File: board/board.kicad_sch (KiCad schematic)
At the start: 0 parts

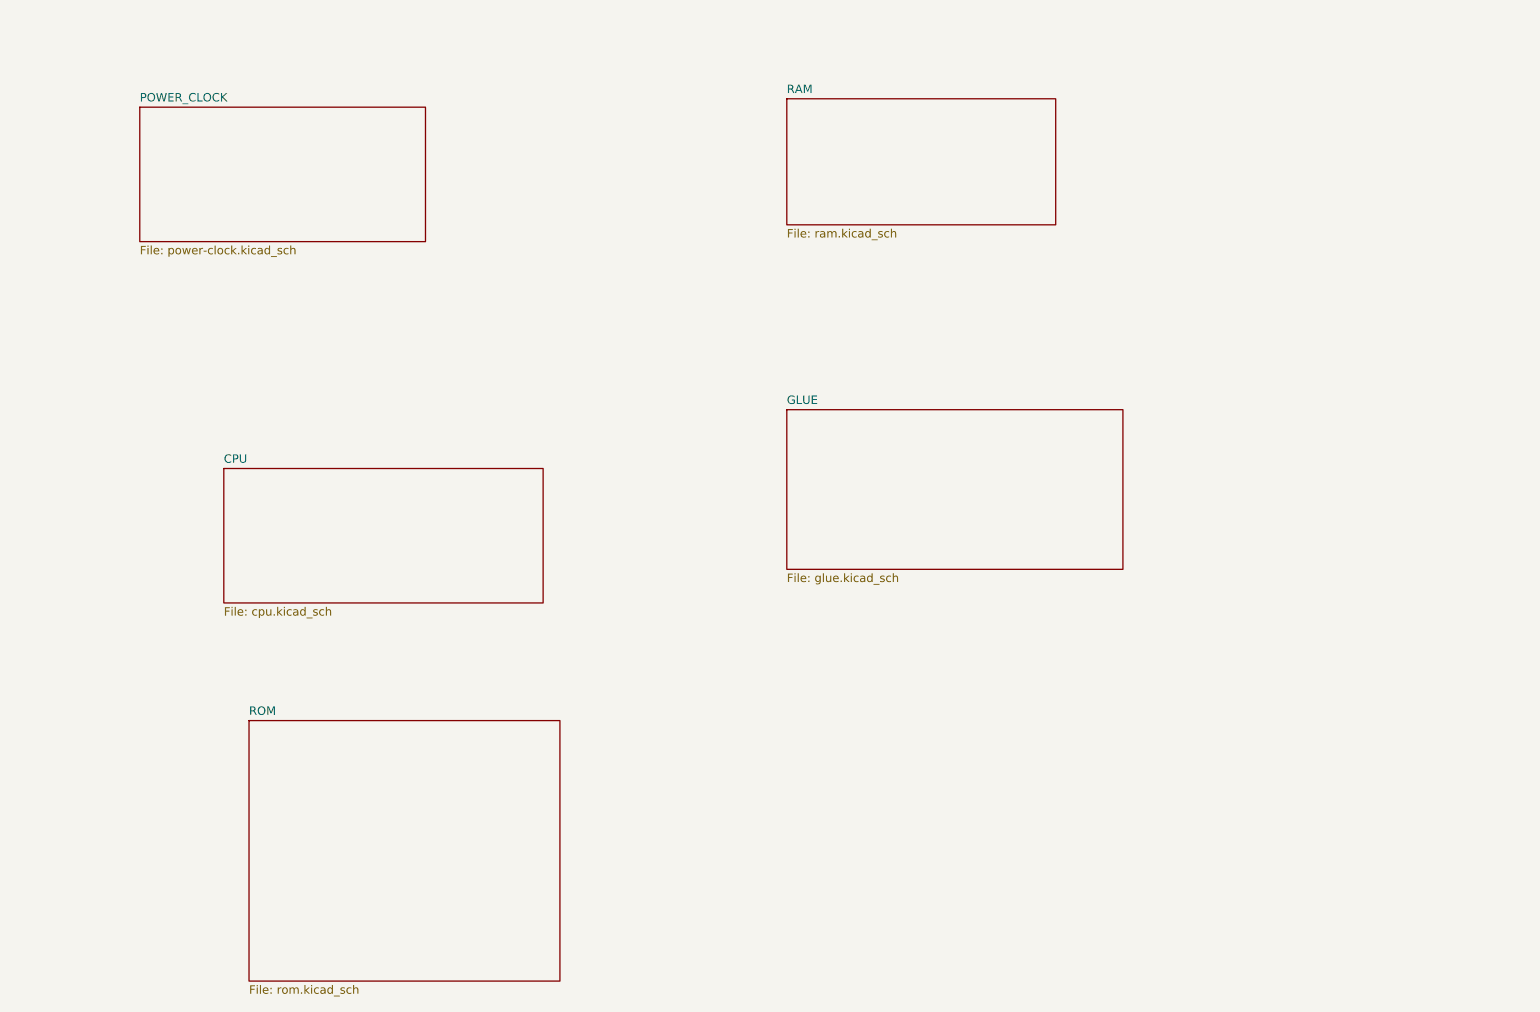
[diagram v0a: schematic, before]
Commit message: fill out most functionality - passes ERC
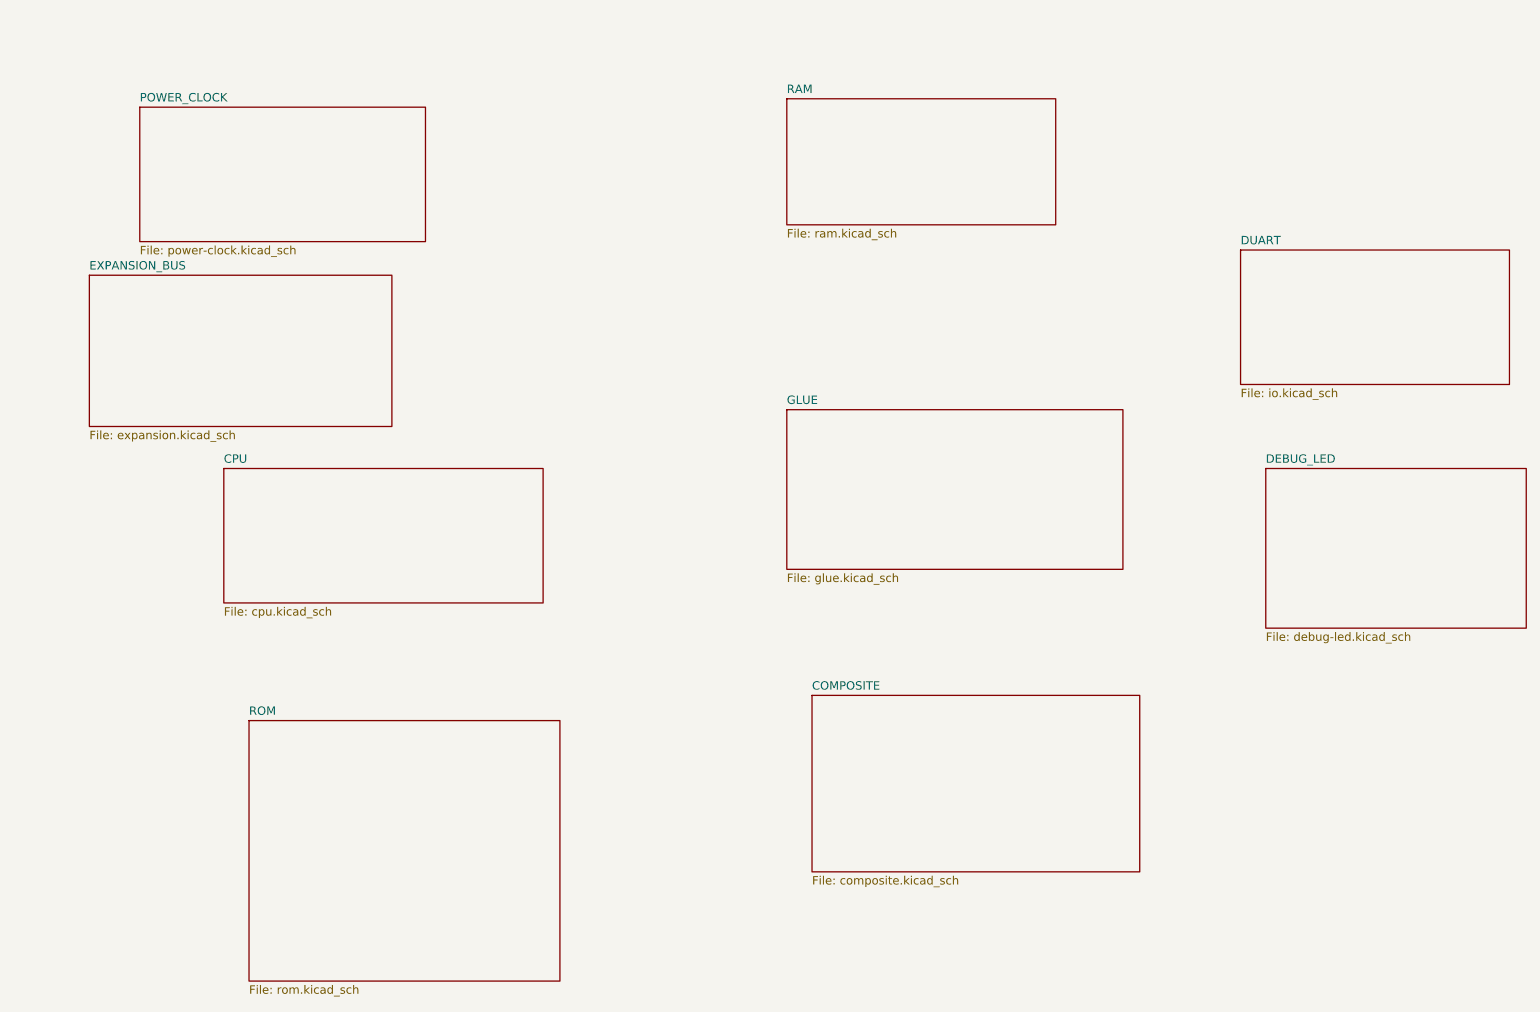
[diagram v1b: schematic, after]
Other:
- added sheet COMPOSITE (composite.kicad_sch)
- added sheet DEBUG_LED (debug-led.kicad_sch)
- added sheet DUART (io.kicad_sch)
- added sheet EXPANSION_BUS (expansion.kicad_sch)
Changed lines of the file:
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@@
+	)
+	(sheet
+		(at 142.24 125.73)
+		(size 49.53 26.67)
+		(exclude_from_sim no)
+		(in_bom yes)
+		(on_board yes)
+		(dnp no)
+		(fields_autoplaced yes)
+		(stroke
+			(width 0.1524)
+			(type solid)
+		)
+		(fill
+			(color 0 0 0 0.0000)
+		)
+		(property "Sheetname" "COMPOSITE"
+			(at 142.24 125.0184 0)
+			(effects
+				(font
+					(size 1.27 1.27)
+				)
+				(justify left bottom)
+			)
+		)
+		(property "Sheetfile" "composite.kicad_sch"
+			(at 142.24 152.9846 0)
+			(effects
+				(font
+					(size 1.27 1.27)
+				)
+				(justify left top)
+			)
+		)
+		(instances
+			(project "board"
+				(path "/afefa398-9f39-4b22-97f8-dae9b102df0d"
+					(page "8")
+				)
+			)
+		)
 	)
 	(sheet
@@
 	)
 	(sheet
+		(at 207.01 58.42)
+		(size 40.64 20.32)
+		(exclude_from_sim no)
+		(in_bom yes)
+		(on_board yes)
+		(dnp no)
+		(fields_autoplaced yes)
+		(stroke
+			(width 0.1524)
+			(type solid)
+		)
+		(fill
+			(color 0 0 0 0.0000)
+		)
+		(property "Sheetname" "DUART"
+			(at 207.01 57.7084 0)
+			(effects
+				(font
+					(size 1.27 1.27)
+				)
+				(justify left bottom)
+			)
+		)
+		(property "Sheetfile" "io.kicad_sch"
+			(at 207.01 79.3246 0)
+			(effects
+				(font
+					(size 1.27 1.27)
+				)
+				(justify left top)
+			)
+		)
+		(instances
+			(project "board"
+				(path "/afefa398-9f39-4b22-97f8-dae9b102df0d"
+					(page "7")
+				)
+			)
+		)
+	)
+	(sheet
+		(at 33.02 62.23)
+		(size 45.72 22.86)
+		(exclude_from_sim no)
+		(in_bom yes)
+		(on_board yes)
+		(dnp no)
+		(fields_autoplaced yes)
+		(stroke
+			(width 0.1524)
+			(type solid)
+		)
+		(fill
+			(color 0 0 0 0.0000)
+		)
+		(property "Sheetname" "EXPANSION_BUS"
+			(at 33.02 61.5184 0)
+			(effects
+				(font
+					(size 1.27 1.27)
+				)
+				(justify left bottom)
+			)
+		)
+		(property "Sheetfile" "expansion.kicad_sch"
+			(at 33.02 85.6746 0)
+			(effects
+				(font
+					(size 1.27 1.27)
+				)
+				(justify left top)
+			)
+		)
+		(instances
+			(project "board"
+				(path "/afefa398-9f39-4b22-97f8-dae9b102df0d"
+					(page "10")
+				)
+			)
+		)
+	)
+	(sheet
 		(at 138.43 35.56)
 		(size 40.64 19.05)
@@
 				)
 			)
+		)
+	)
+	(sheet
+		(at 210.82 91.44)
+		(size 39.37 24.13)
+		(exclude_from_sim no)
+		(in_bom yes)
+		(on_board yes)
+		(dnp no)
+		(fields_autoplaced yes)
+		(stroke
+			(width 0.1524)
+			(type solid)
+		)
+		(fill
+			(color 0 0 0 0.0000)
+		)
+		(property "Sheetname" "DEBUG_LED"
+			(at 210.82 90.7284 0)
+			(effects
+				(font
+					(size 1.27 1.27)
+				)
+				(justify left bottom)
+			)
+		)
+		(property "Sheetfile" "debug-led.kicad_sch"
+			(at 210.82 116.1546 0)
+			(effects
+				(font
+					(size 1.27 1.27)
+				)
+				(justify left top)
+			)
+		)
+		(instances
+			(project "board"
+				(path "/afefa398-9f39-4b22-97f8-dae9b102df0d"
+					(page "9")
+				)
+			)

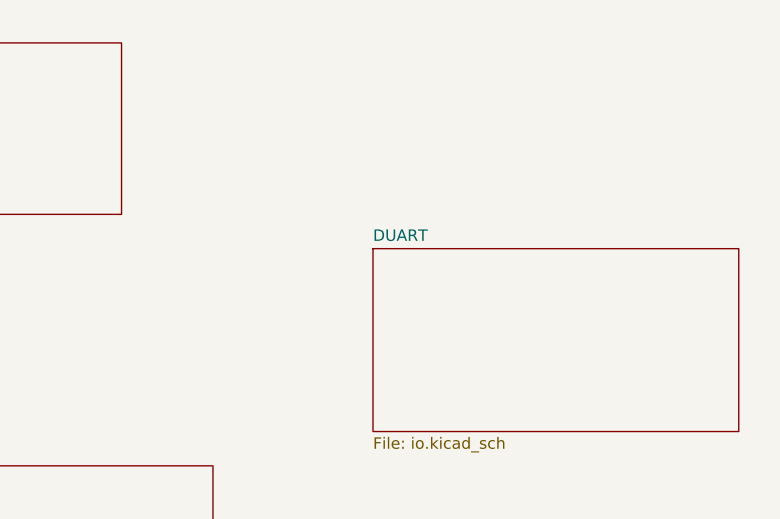
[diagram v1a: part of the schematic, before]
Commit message: change IO to 8051 variant, add audio
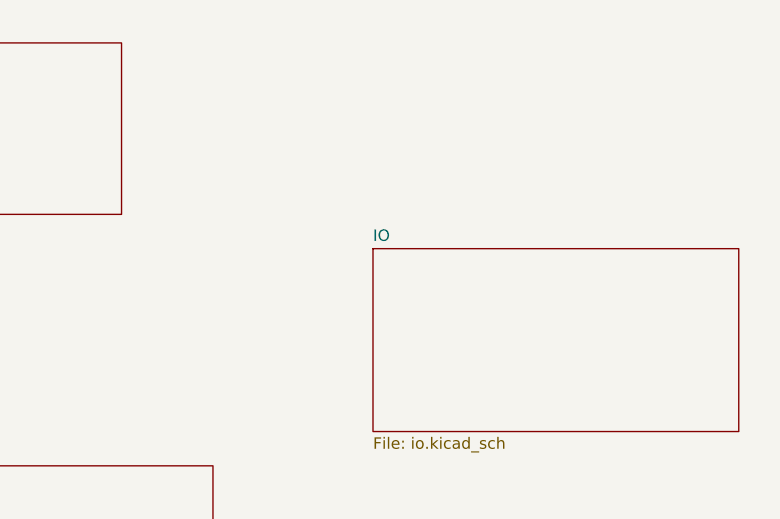
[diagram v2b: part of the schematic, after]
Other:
- sheet DUART renamed IO
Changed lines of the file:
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@@
 			(color 0 0 0 0.0000)
 		)
-		(property "Sheetname" "DUART"
+		(property "Sheetname" "IO"
 			(at 207.01 57.7084 0)
 			(effects

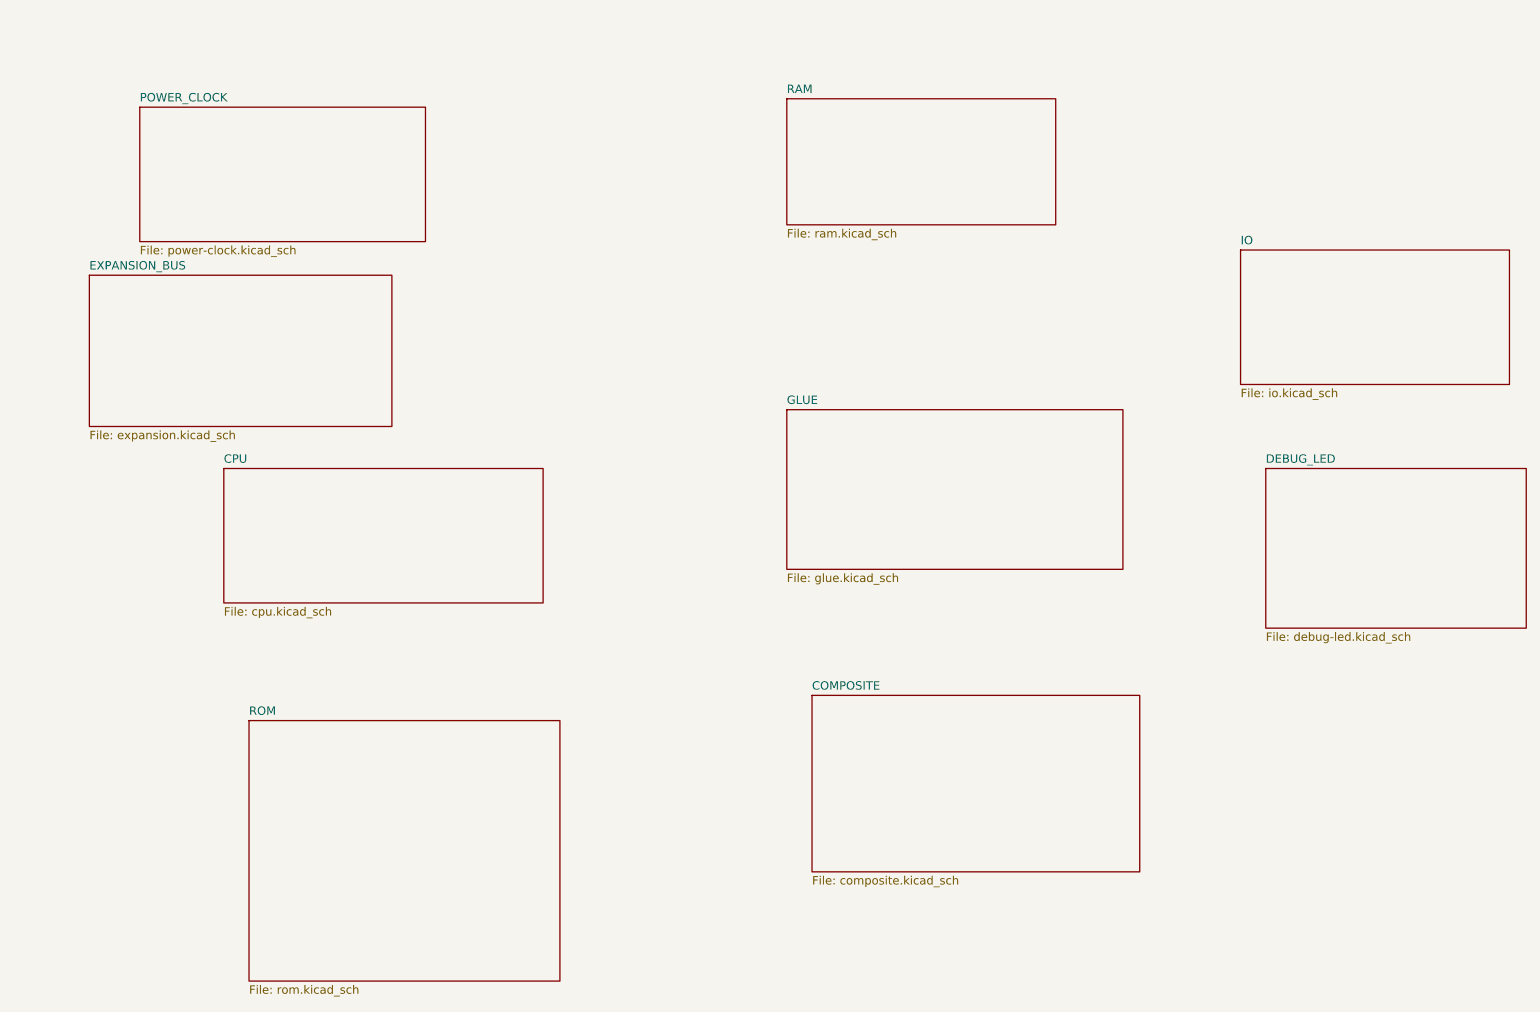
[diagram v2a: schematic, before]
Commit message: start of PCB and MMU
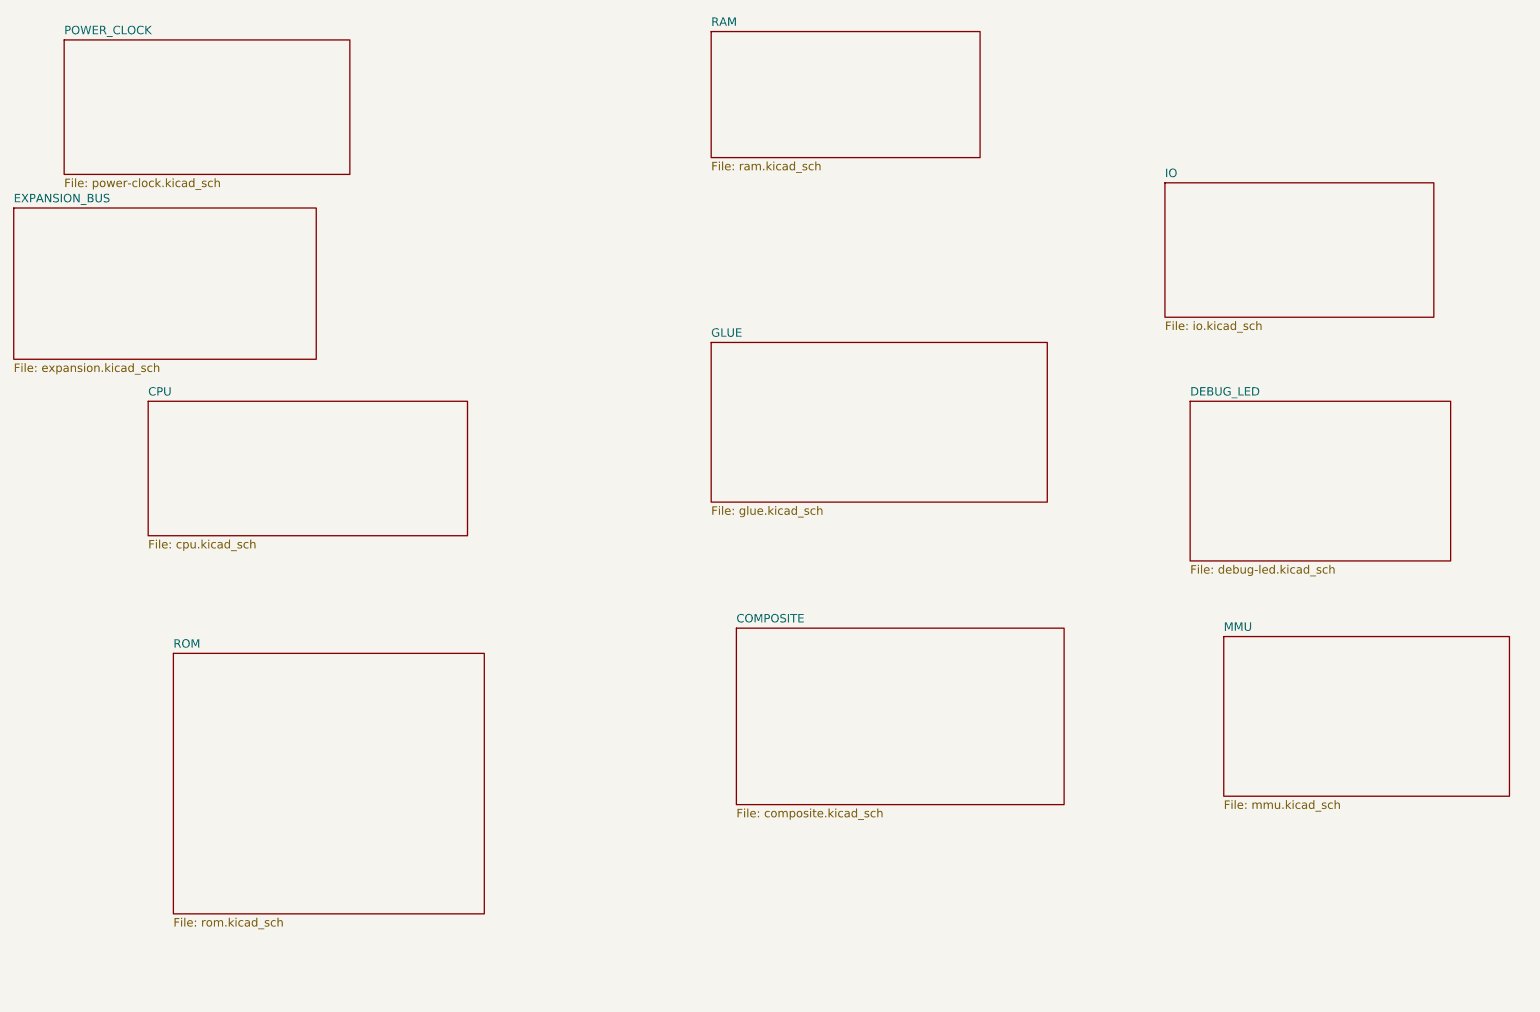
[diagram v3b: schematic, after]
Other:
- added sheet MMU (mmu.kicad_sch)
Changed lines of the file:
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@@
 	(paper "A4")
 	(sheet
-		(at 138.43 82.55)
+		(at 127 72.39)
 		(size 50.8 24.13)
 		(exclude_from_sim no)
@@
 		)
 		(property "Sheetname" "GLUE"
-			(at 138.43 81.8384 0)
+			(at 127 71.6784 0)
 			(effects
 				(font
@@
 		)
 		(property "Sheetfile" "glue.kicad_sch"
-			(at 138.43 107.2646 0)
+			(at 127 97.1046 0)
 			(effects
 				(font
@@
 	)
 	(sheet
-		(at 142.24 125.73)
+		(at 130.81 115.57)
 		(size 49.53 26.67)
 		(exclude_from_sim no)
@@
 		)
 		(property "Sheetname" "COMPOSITE"
-			(at 142.24 125.0184 0)
+			(at 130.81 114.8584 0)
 			(effects
 				(font
@@
 		)
 		(property "Sheetfile" "composite.kicad_sch"
-			(at 142.24 152.9846 0)
+			(at 130.81 142.8246 0)
 			(effects
 				(font
@@
 	)
 	(sheet
-		(at 57.15 129.54)
+		(at 45.72 119.38)
 		(size 46.99 39.37)
 		(exclude_from_sim no)
@@
 		)
 		(property "Sheetname" "ROM"
-			(at 57.15 128.8284 0)
+			(at 45.72 118.6684 0)
 			(effects
 				(font
@@
 		)
 		(property "Sheetfile" "rom.kicad_sch"
-			(at 57.15 169.4946 0)
+			(at 45.72 159.3346 0)
 			(effects
 				(font
@@
 	)
 	(sheet
-		(at 40.64 36.83)
+		(at 29.21 26.67)
 		(size 43.18 20.32)
 		(exclude_from_sim no)
@@
 		)
 		(property "Sheetname" "POWER_CLOCK"
-			(at 40.64 36.1184 0)
+			(at 29.21 25.9584 0)
 			(effects
 				(font
@@
 		)
 		(property "Sheetfile" "power-clock.kicad_sch"
-			(at 40.64 57.7346 0)
+			(at 29.21 47.5746 0)
 			(effects
 				(font
@@
 	)
 	(sheet
-		(at 207.01 58.42)
+		(at 195.58 48.26)
 		(size 40.64 20.32)
 		(exclude_from_sim no)
@@
 		)
 		(property "Sheetname" "IO"
-			(at 207.01 57.7084 0)
+			(at 195.58 47.5484 0)
 			(effects
 				(font
@@
 		)
 		(property "Sheetfile" "io.kicad_sch"
-			(at 207.01 79.3246 0)
+			(at 195.58 69.1646 0)
 			(effects
 				(font
@@
 	)
 	(sheet
-		(at 33.02 62.23)
+		(at 21.59 52.07)
 		(size 45.72 22.86)
 		(exclude_from_sim no)
@@
 		)
 		(property "Sheetname" "EXPANSION_BUS"
-			(at 33.02 61.5184 0)
+			(at 21.59 51.3584 0)
 			(effects
 				(font
@@
 		)
 		(property "Sheetfile" "expansion.kicad_sch"
-			(at 33.02 85.6746 0)
+			(at 21.59 75.5146 0)
 			(effects
 				(font
@@
 	)
 	(sheet
-		(at 138.43 35.56)
+		(at 127 25.4)
 		(size 40.64 19.05)
 		(exclude_from_sim no)
@@
 		)
 		(property "Sheetname" "RAM"
-			(at 138.43 34.8484 0)
+			(at 127 24.6884 0)
 			(effects
 				(font
@@
 		)
 		(property "Sheetfile" "ram.kicad_sch"
-			(at 138.43 55.1946 0)
+			(at 127 45.0346 0)
 			(effects
 				(font
@@
 	)
 	(sheet
-		(at 53.34 91.44)
+		(at 41.91 81.28)
 		(size 48.26 20.32)
 		(exclude_from_sim no)
@@
 		)
 		(property "Sheetname" "CPU"
-			(at 53.34 90.7284 0)
+			(at 41.91 80.5684 0)
 			(effects
 				(font
@@
 		)
 		(property "Sheetfile" "cpu.kicad_sch"
-			(at 53.34 112.3446 0)
+			(at 41.91 102.1846 0)
 			(effects
 				(font
@@
 	)
 	(sheet
-		(at 210.82 91.44)
+		(at 199.39 81.28)
 		(size 39.37 24.13)
 		(exclude_from_sim no)
@@
 		)
 		(property "Sheetname" "DEBUG_LED"
-			(at 210.82 90.7284 0)
+			(at 199.39 80.5684 0)
 			(effects
 				(font
@@
 		)
 		(property "Sheetfile" "debug-led.kicad_sch"
-			(at 210.82 116.1546 0)
+			(at 199.39 105.9946 0)
 			(effects
 				(font
@@
 				)
 			)
+		)
+	)
+	(sheet
+		(at 204.47 116.84)
+		(size 43.18 24.13)
+		(exclude_from_sim no)
+		(in_bom yes)
+		(on_board yes)
+		(dnp no)
+		(fields_autoplaced yes)
+		(stroke
+			(width 0.1524)
+			(type solid)
+		)
+		(fill
+			(color 0 0 0 0.0000)
+		)
+		(property "Sheetname" "MMU"
+			(at 204.47 116.1284 0)
+			(effects
+				(font
+					(size 1.27 1.27)
+				)
+				(justify left bottom)
+			)
+		)
+		(property "Sheetfile" "mmu.kicad_sch"
+			(at 204.47 141.5546 0)
+			(effects
+				(font
+					(size 1.27 1.27)
+				)
+				(justify left top)
+			)
+		)
+		(instances
+			(project "board"
+				(path "/afefa398-9f39-4b22-97f8-dae9b102df0d"
+					(page "11")
+				)
+			)

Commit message: checkpoint
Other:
- removed sheet MMU
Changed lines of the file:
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@@
-		)
-	)
-	(sheet
-		(at 204.47 116.84)
-		(size 43.18 24.13)
-		(exclude_from_sim no)
-		(in_bom yes)
-		(on_board yes)
-		(dnp no)
-		(fields_autoplaced yes)
-		(stroke
-			(width 0.1524)
-			(type solid)
-		)
-		(fill
-			(color 0 0 0 0.0000)
-		)
-		(property "Sheetname" "MMU"
-			(at 204.47 116.1284 0)
-			(effects
-				(font
-					(size 1.27 1.27)
-				)
-				(justify left bottom)
-			)
-		)
-		(property "Sheetfile" "mmu.kicad_sch"
-			(at 204.47 141.5546 0)
-			(effects
-				(font
-					(size 1.27 1.27)
-				)
-				(justify left top)
-			)
-		)
-		(instances
-			(project "board"
-				(path "/afefa398-9f39-4b22-97f8-dae9b102df0d"
-					(page "11")
-				)
-			)
 		)
 	)
